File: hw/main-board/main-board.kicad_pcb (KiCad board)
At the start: 0 parts

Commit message: Add board outline (Edge.Cuts) to main-board
Fixes the invalid_outline DRC error (no closed outline on Edge.Cuts).
Also ignore .history/ (editor local-history artifacts, not project
data).
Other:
- board outline added: 93.5 x 66.5 mm
- copper layers 0 -> 2
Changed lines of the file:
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@@
-(kicad_pcb (version 20260206) (generator "pcbnew") (generator_version "10.0")
+(kicad_pcb
+	(version 20260206)
+	(generator "pcbnew")
+	(generator_version "10.0")
+	(general
+		(thickness 1.6)
+		(legacy_teardrops no)
+	)
+	(paper "A4")
 	(title_block
 		(rev "${REVISION}")
 	)
+	(layers
+		(0 "F.Cu" signal)
+		(2 "B.Cu" signal)
+		(9 "F.Adhes" user "F.Adhesive")
+		(11 "B.Adhes" user "B.Adhesive")
+		(13 "F.Paste" user)
+		(15 "B.Paste" user)
+		(5 "F.SilkS" user "F.Silkscreen")
+		(7 "B.SilkS" user "B.Silkscreen")
+		(1 "F.Mask" user)
+		(3 "B.Mask" user)
+		(17 "Dwgs.User" user "User.Drawings")
+		(19 "Cmts.User" user "User.Comments")
+		(21 "Eco1.User" user "User.Eco1")
+		(23 "Eco2.User" user "User.Eco2")
+		(25 "Edge.Cuts" user)
+		(27 "Margin" user)
+		(31 "F.CrtYd" user "F.Courtyard")
+		(29 "B.CrtYd" user "B.Courtyard")
+		(35 "F.Fab" user)
+		(33 "B.Fab" user)
+		(39 "User.1" user)
+		(41 "User.2" user)
+		(43 "User.3" user)
+		(45 "User.4" user)
+	)
+	(setup
+		(pad_to_mask_clearance 0)
+		(allow_soldermask_bridges_in_footprints no)
+		(tenting
+			(front yes)
+			(back yes)
+		)
+		(covering
+			(front no)
+			(back no)
+		)
+		(plugging
+			(front no)
+			(back no)
+		)
+		(capping no)
+		(filling no)
+		(pcbplotparams
+			(layerselection 0x00000000_00000000_55555555_5755f5ff)
+			(plot_on_all_layers_selection 0x00000000_00000000_00000000_00000000)
+			(disableapertmacros no)
+			(usegerberextensions no)
+			(usegerberattributes yes)
+			(usegerberadvancedattributes yes)
+			(creategerberjobfile yes)
+			(dashed_line_dash_ratio 12)
+			(dashed_line_gap_ratio 3)
+			(svgprecision 4)
+			(plotframeref no)
+			(mode 1)
+			(useauxorigin no)
+			(pdf_front_fp_property_popups yes)
+			(pdf_back_fp_property_popups yes)
+			(pdf_metadata yes)
+			(pdf_single_document no)
+			(dxfpolygonmode yes)
+			(dxfimperialunits yes)
+			(dxfusepcbnewfont yes)
+			(psnegative no)
+			(psa4output no)
+			(plot_black_and_white yes)
+			(sketchpadsonfab no)
+			(plotpadnumbers no)
+			(hidednponfab no)
+			(sketchdnponfab yes)
+			(crossoutdnponfab yes)
+			(subtractmaskfromsilk no)
+			(outputformat 1)
+			(mirror no)
+			(drillshape 1)
+			(scaleselection 1)
+			(outputdirectory "")
+		)
+	)
+	(gr_rect
+		(start 88.5 49)
+		(end 182 115.5)
+		(stroke
+			(width 0.05)
+			(type default)
+		)
+		(fill no)
+		(layer "Edge.Cuts")
+	)
+	(embedded_fonts no)
 )

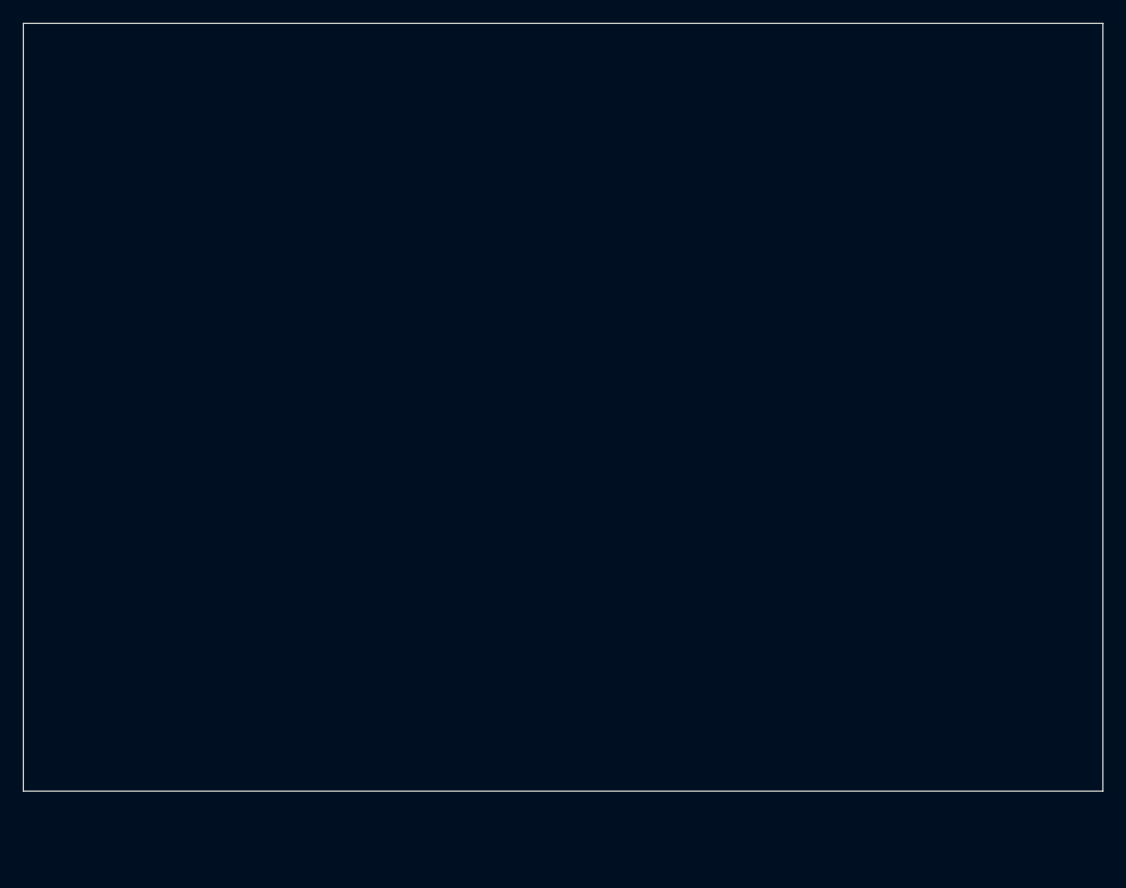
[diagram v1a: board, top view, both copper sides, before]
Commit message: Add PTR54L power circuit and initial PCB outline with placed components
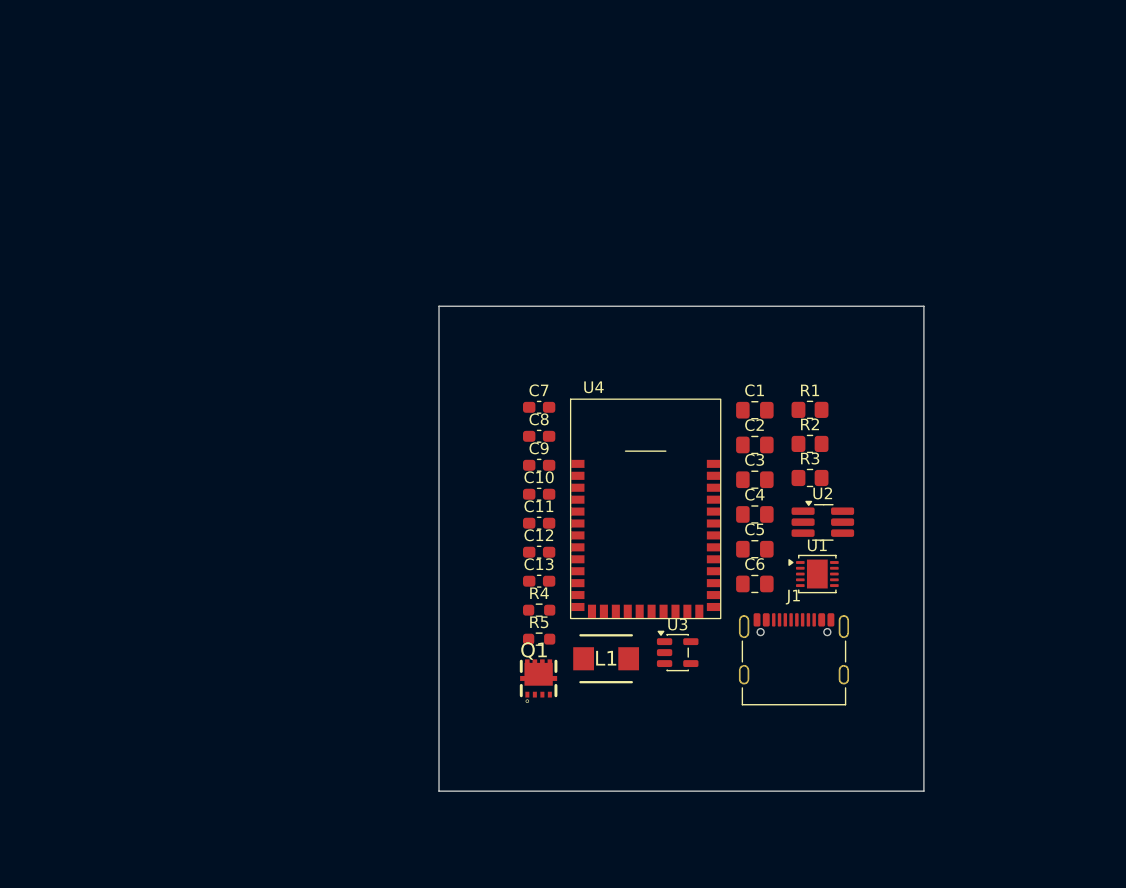
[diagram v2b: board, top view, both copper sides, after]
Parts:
- added C1: 4.7uF, Capacitor_SMD:C_0805_2012Metric_Pad1.18x1.45mm_HandSolder, F.Cu at (151.9, 82.5)
- added C10: 4.7uF, Capacitor_SMD:C_0603_1608Metric_Pad1.08x0.95mm_HandSolder, F.Cu at (133.2, 89.8)
- added C11: 4.7uF, Capacitor_SMD:C_0603_1608Metric_Pad1.08x0.95mm_HandSolder, F.Cu at (133.2, 92.3)
- added C12: 100nF, Capacitor_SMD:C_0603_1608Metric_Pad1.08x0.95mm_HandSolder, F.Cu at (133.2, 94.8)
- added C13: 22uF, Capacitor_SMD:C_0603_1608Metric_Pad1.08x0.95mm_HandSolder, F.Cu at (133.2, 97.3)
- added C2: 4.7uF, Capacitor_SMD:C_0805_2012Metric_Pad1.18x1.45mm_HandSolder, F.Cu at (151.9, 85.5)
- added C3: 4.7uF, Capacitor_SMD:C_0805_2012Metric_Pad1.18x1.45mm_HandSolder, F.Cu at (151.9, 88.5)
- added C4: 4.7uF, Capacitor_SMD:C_0805_2012Metric_Pad1.18x1.45mm_HandSolder, F.Cu at (151.9, 91.5)
- added C5: 4.7uF, Capacitor_SMD:C_0805_2012Metric_Pad1.18x1.45mm_HandSolder, F.Cu at (151.9, 94.5)
- added C6: 4.7uF, Capacitor_SMD:C_0805_2012Metric_Pad1.18x1.45mm_HandSolder, F.Cu at (151.9, 97.6)
- added C7: 0.1uF, Capacitor_SMD:C_0603_1608Metric_Pad1.08x0.95mm_HandSolder, F.Cu at (133.2, 82.3)
- added C8: 22uF, Capacitor_SMD:C_0603_1608Metric_Pad1.08x0.95mm_HandSolder, F.Cu at (133.2, 84.8)
- added C9: 22uF, Capacitor_SMD:C_0603_1608Metric_Pad1.08x0.95mm_HandSolder, F.Cu at (133.2, 87.3)
- added J1: USB_C_Receptacle_USB2.0_16P, Connector_USB:USB_C_Receptacle_Palconn_UTC16-G, F.Cu at (155.2, 103.2)
- added L1: IHLP1616BZER4R7M11, Samacsys:INDPM4441X200N, F.Cu at (139.0, 104.0)
- added Q1: AONR21307, Samacsys:DFN_3X3_EP, F.Cu at (133.1, 105.7)
- added R1: 10R, Resistor_SMD:R_0805_2012Metric_Pad1.20x1.40mm_HandSolder, F.Cu at (156.6, 82.5)
- added R2: 5K1, Resistor_SMD:R_0805_2012Metric_Pad1.20x1.40mm_HandSolder, F.Cu at (156.6, 85.4)
- added R3: 49K9, Resistor_SMD:R_0805_2012Metric_Pad1.20x1.40mm_HandSolder, F.Cu at (156.6, 88.4)
- added R4: 10R, Resistor_SMD:R_0603_1608Metric_Pad0.98x0.95mm_HandSolder, F.Cu at (133.2, 99.8)
- added R5: 10R, Resistor_SMD:R_0603_1608Metric_Pad0.98x0.95mm_HandSolder, F.Cu at (133.2, 102.3)
- added U1: HUSB238_xxxDD, Package_DFN_QFN:WDFN-10-1EP_3x3mm_P0.5mm_EP1.8x2.5mm, F.Cu at (157.3, 96.7)
- added U2: AP63205WU, Package_TO_SOT_SMD:TSOT-23-6_HandSoldering, F.Cu at (157.7, 92.2)
- added U3: AP2112K-3.3, Package_TO_SOT_SMD:SOT-23-5, F.Cu at (145.2, 103.5)
- added U4: PTR54L, Project_Specific_Parts:PTR54L15, F.Cu at (142.4, 91.0)
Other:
- board size 93.5 x 66.5 mm -> 42 x 42 mm

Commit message: 3D model for TMC2226 added
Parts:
- added U5: TMC2226-SA, Package_SO:HTSSOP-28-1EP_4.4x9.7mm_P0.65mm_EP2.75x6.2mm_ThermalVias, F.Cu at (142.2, 110.6)
- C12: value 100nF -> 0.1uF

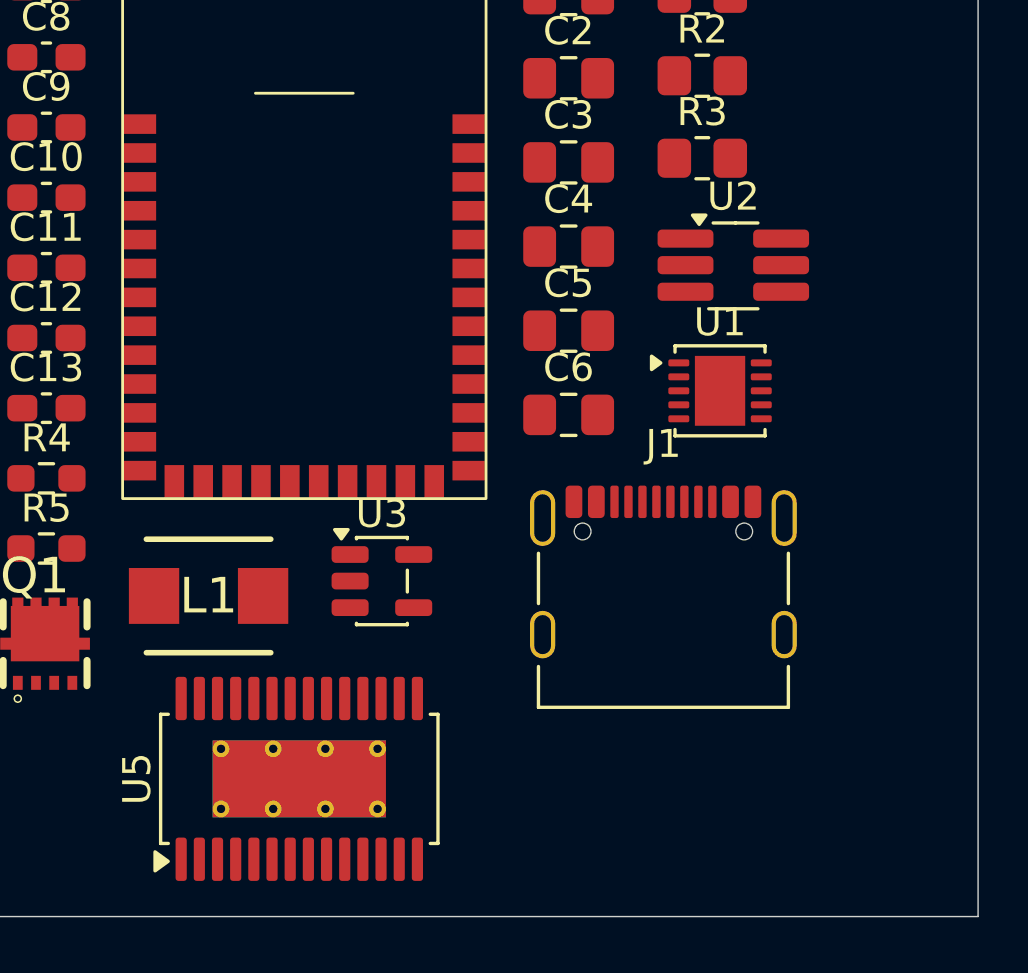
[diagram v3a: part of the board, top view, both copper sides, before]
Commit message: Add 3d model for WDFN10 component, change footprint for 5V buck converter
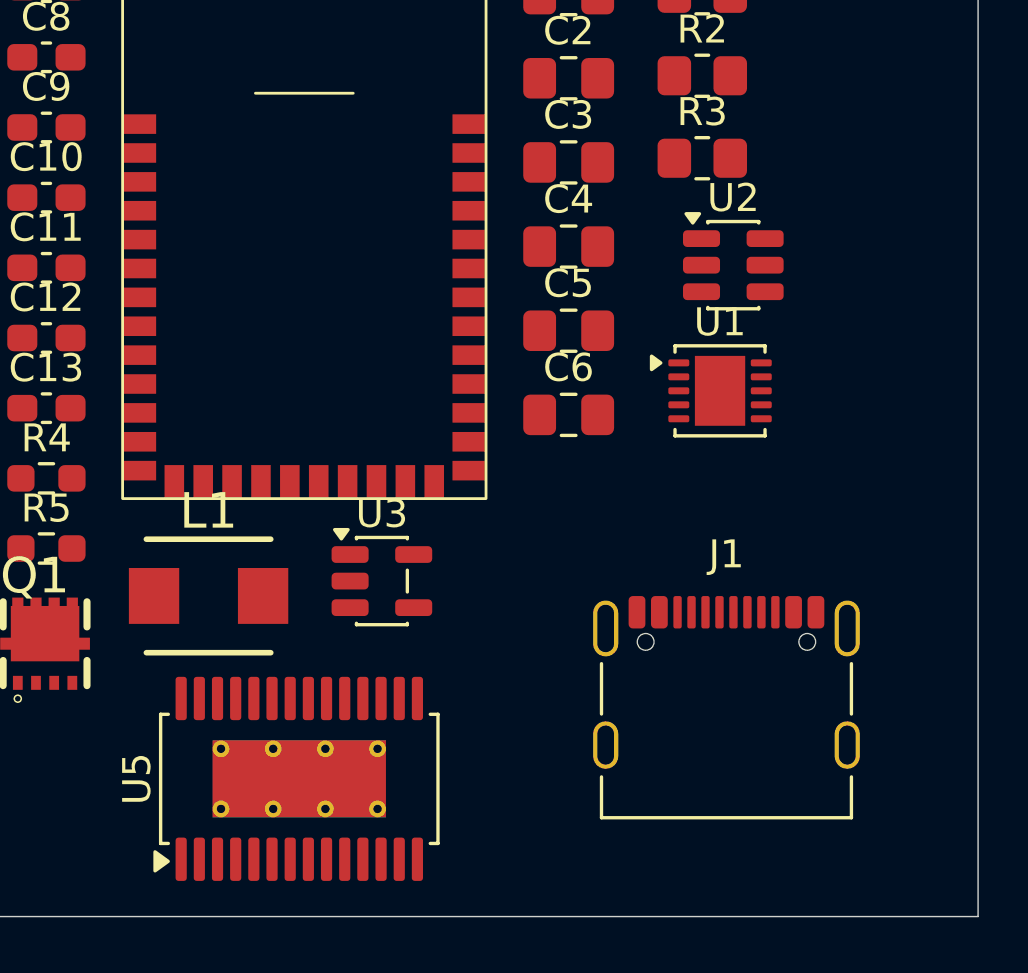
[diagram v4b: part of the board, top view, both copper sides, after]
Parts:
- U2: footprint Package_TO_SOT_SMD:TSOT-23-6_HandSoldering -> Package_TO_SOT_SMD:TSOT-23-6
- moved J1 4.55 mm to (157.5, 107.1)
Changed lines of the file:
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@@
 		)
 	)
-	(footprint "Package_TO_SOT_SMD:TSOT-23-6_HandSoldering"
+	(footprint "Package_TO_SOT_SMD:TSOT-23-6"
 		(layer "F.Cu")
 		(at 157.745 92.2)
-		(descr "6-pin TSOT23 package, http://cds.linear.com/docs/en/packaging/SOT_6_05-08-1636.pdf")
-		(tags "TSOT-23-6 MK06A TSOT-6 Hand-soldering")
+		(descr "TSOT, 6 Pin (https://www.jedec.org/sites/default/files/docs/MO-193D.pdf variant AA)")
+		(tags "TSOT TO_SOT_SMD")
 		(property "Reference" "U2"
-			(at 0 -2.45 0)
+			(at 0 -2.4 0)
 			(layer "F.SilkS")
 			(effects
@@
 		)
 		(property "Value" "AP63205WU"
-			(at 0 2.5 0)
+			(at 0 2.4 0)
 			(layer "F.Fab")
 			(effects
@@
 		(property "Datasheet" "https://www.diodes.com/assets/Datasheets/AP63200-AP63201-AP63203-AP63205.pdf"
 			(at 0 0 0)
-			(unlocked yes)
 			(layer "F.Fab")
 			(hide yes)
@@
 				(font
 					(size 1.27 1.27)
-					(thickness 0.15)
 				)
 			)
@@
 		(property "Description" "2A, 1.1MHz Buck DC/DC Converter, fixed 5.0V output voltage, TSOT-23-6"
 			(at 0 0 0)
-			(unlocked yes)
 			(layer "F.Fab")
 			(hide yes)
@@
 				(font
 					(size 1.27 1.27)
+				)
+			)
+		)
+		(property "KiLib_Generator" "package/gullwing"
+			(at 0 0 0)
+			(layer "F.SilkS")
+			(hide yes)
+			(effects
+				(font
+					(size 1 1)
 					(thickness 0.15)
 				)
@@
 		(duplicate_pad_numbers_are_jumpers no)
 		(fp_line
-			(start -0.88 1.56)
-			(end 0.88 1.56)
+			(start -0.91 -1.56)
+			(end 0.91 -1.56)
 			(stroke
 				(width 0.12)
@@
 		)
 		(fp_line
-			(start 0.08 -1.51)
-			(end -0.72 -1.51)
+			(start -0.91 -1.51)
+			(end -0.91 -1.56)
 			(stroke
 				(width 0.12)
@@
 		)
 		(fp_line
-			(start 0.08 -1.51)
-			(end 0.88 -1.51)
+			(start -0.91 1.56)
+			(end -0.91 1.51)
+			(stroke
+				(width 0.12)
+				(type solid)
+			)
+			(layer "F.SilkS")
+		)
+		(fp_line
+			(start 0.91 -1.56)
+			(end 0.91 -1.51)
+			(stroke
+				(width 0.12)
+				(type solid)
+			)
+			(layer "F.SilkS")
+		)
+		(fp_line
+			(start 0.91 1.51)
+			(end 0.91 1.56)
+			(stroke
+				(width 0.12)
+				(type solid)
+			)
+			(layer "F.SilkS")
+		)
+		(fp_line
+			(start 0.91 1.56)
+			(end -0.91 1.56)
 			(stroke
 				(width 0.12)
@@
 		(fp_poly
 			(pts
-				(xy -1.22 -1.46) (xy -1.46 -1.79) (xy -0.98 -1.79) (xy -1.22 -1.46)
+				(xy -1.45 -1.51) (xy -1.69 -1.84) (xy -1.21 -1.84)
 			)
 			(stroke
@@
 		)
 		(fp_line
-			(start -2.96 -1.7)
-			(end -2.96 1.7)
+			(start -2.05 -1.5)
+			(end -1.05 -1.5)
 			(stroke
 				(width 0.05)
@@
 		)
 		(fp_line
-			(start -2.96 -1.7)
-			(end 2.96 -1.7)
+			(start -2.05 1.5)
+			(end -2.05 -1.5)
 			(stroke
 				(width 0.05)
@@
 		)
 		(fp_line
-			(start 2.96 1.7)
-			(end -2.96 1.7)
+			(start -1.05 -1.7)
+			(end 1.05 -1.7)
 			(stroke
 				(width 0.05)
@@
 		)
 		(fp_line
-			(start 2.96 1.7)
-			(end 2.96 -1.7)
+			(start -1.05 -1.5)
+			(end -1.05 -1.7)
 			(stroke
 				(width 0.05)
@@
 		)
 		(fp_line
-			(start -0.88 -1)
-			(end -0.88 1.45)
+			(start -1.05 1.5)
+			(end -2.05 1.5)
 			(stroke
-				(width 0.1)
+				(width 0.05)
 				(type solid)
 			)
-			(layer "F.Fab")
+			(layer "F.CrtYd")
 		)
 		(fp_line
-			(start -0.88 -1)
-			(end -0.43 -1.45)
+			(start -1.05 1.7)
+			(end -1.05 1.5)
 			(stroke
-				(width 0.1)
+				(width 0.05)
 				(type solid)
 			)
-			(layer "F.Fab")
+			(layer "F.CrtYd")
 		)
 		(fp_line
-			(start 0.88 -1.45)
-			(end -0.43 -1.45)
+			(start 1.05 -1.7)
+			(end 1.05 -1.5)
 			(stroke
-				(width 0.1)
+				(width 0.05)
 				(type solid)
 			)
-			(layer "F.Fab")
+			(layer "F.CrtYd")
 		)
 		(fp_line
-			(start 0.88 -1.45)
-			(end 0.88 1.45)
+			(start 1.05 -1.5)
+			(end 2.05 -1.5)
 			(stroke
-				(width 0.1)
+				(width 0.05)
 				(type solid)
 			)
-			(layer "F.Fab")
+			(layer "F.CrtYd")
+		)
+		(fp_line
+			(start 1.05 1.5)
+			(end 1.05 1.7)
+			(stroke
+				(width 0.05)
+				(type solid)
+			)
+			(layer "F.CrtYd")
+		)
+		(fp_line
+			(start 1.05 1.7)
+			(end -1.05 1.7)
+			(stroke
+				(width 0.05)
+				(type solid)
+			)
+			(layer "F.CrtYd")
+		)
+		(fp_line
+			(start 2.05 -1.5)
+			(end 2.05 1.5)
+			(stroke
+				(width 0.05)
+				(type solid)
+			)
+			(layer "F.CrtYd")
 		)
 		(fp_line
-			(start 0.88 1.45)
-			(end -0.88 1.45)
+			(start 2.05 1.5)
+			(end 1.05 1.5)
+			(stroke
+				(width 0.05)
+				(type solid)
+			)
+			(layer "F.CrtYd")
+		)
+		(fp_poly
+			(pts
+				(xy -0.4 -1.45) (xy 0.8 -1.45) (xy 0.8 1.45) (xy -0.8 1.45) (xy -0.8 -1.05)
+			)
 			(stroke
 				(width 0.1)
 				(type solid)
 			)
+			(fill no)
 			(layer "F.Fab")
 		)
@@
 			(effects
 				(font
-					(size 0.5 0.5)
-					(thickness 0.075)
+					(size 0.72 0.72)
+					(thickness 0.11)
 				)
 			)
 		)
 		(pad "1" smd roundrect
-			(at -1.71 -0.95)
-			(size 2 0.65)
+			(at -1.1375 -0.95)
+			(size 1.325 0.6)
 			(layers "F.Cu" "F.Mask" "F.Paste")
 			(roundrect_rratio 0.25)
@@
 		)
 		(pad "2" smd roundrect
-			(at -1.71 0)
-			(size 2 0.65)
+			(at -1.1375 0)
+			(size 1.325 0.6)
 			(layers "F.Cu" "F.Mask" "F.Paste")
 			(roundrect_rratio 0.25)
@@
 		)
 		(pad "3" smd roundrect
-			(at -1.71 0.95)
-			(size 2 0.65)
+			(at -1.1375 0.95)
+			(size 1.325 0.6)
 			(layers "F.Cu" "F.Mask" "F.Paste")
 			(roundrect_rratio 0.25)
@@
 		)
 		(pad "4" smd roundrect
-			(at 1.71 0.95)
-			(size 2 0.65)
+			(at 1.1375 0.95)
+			(size 1.325 0.6)
 			(layers "F.Cu" "F.Mask" "F.Paste")
 			(roundrect_rratio 0.25)
@@
 		)
 		(pad "5" smd roundrect
-			(at 1.71 0)
-			(size 2 0.65)
+			(at 1.1375 0)
+			(size 1.325 0.6)
 			(layers "F.Cu" "F.Mask" "F.Paste")
 			(roundrect_rratio 0.25)
@@
 		)
 		(pad "6" smd roundrect
-			(at 1.71 -0.95)
-			(size 2 0.65)
+			(at 1.1375 -0.95)
+			(size 1.325 0.6)
 			(layers "F.Cu" "F.Mask" "F.Paste")
 			(roundrect_rratio 0.25)
@@
 		)
 		(embedded_fonts no)
-		(model "${KICAD10_3DMODEL_DIR}/Package_DFN_QFN.3dshapes/WDFN-10-1EP_3x3mm_P0.5mm_EP1.8x2.5mm.step"
+		(model "E:/Projects/Perde/hw/lib/SamacSys_Parts.3dshapes/IQS620A_DFN3X3_21-07-2020.STEP"
 			(offset
-				(xyz 0 0 0)
+				(xyz 0 0 -5)
 			)
 			(scale
@@
 			)
 			(rotate
-				(xyz 0 0 0)
+				(xyz 90 -0 90)
 			)
 		)
@@
 	(footprint "Connector_USB:USB_C_Receptacle_Palconn_UTC16-G"
 		(layer "F.Cu")
-		(at 155.245 103.175)
+		(at 157.5 107.125)
 		(descr "http://www.palpilot.com/wp-content/uploads/2017/05/UTC027-GKN-OR-Rev-A.pdf")
 		(tags "USB C Type-C Receptacle USB2.0")
@@
 		)
 		(embedded_fonts no)
-		(model "${KICAD10_3DMODEL_DIR}/Connector_USB.3dshapes/USB_C_Receptacle_Palconn_UTC16-G.step"
+		(model "${KICAD10_3DMODEL_DIR}/Connector_USB.3dshapes/USB_C_Receptacle_GCT_USB4105-xx-A_16P_TopMnt_Horizontal.step"
 			(offset
-				(xyz 0 0 0)
+				(xyz 0 -1.25 0)
 			)
 			(scale
@@
 			)
 			(rotate
-				(xyz 0 0 0)
+				(xyz -0 -0 -0)
 			)
 		)
@@
 		(tags "Inductor")
 		(property "Reference" "L1"
-			(at 0 0 0)
+			(at 0 -3.032 0)
 			(layer "F.SilkS")
 			(effects
